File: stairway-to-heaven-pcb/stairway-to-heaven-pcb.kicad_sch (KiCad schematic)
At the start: 1 part, among them U1 MEGA_PRO_EMBED_CH340G_{slash}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

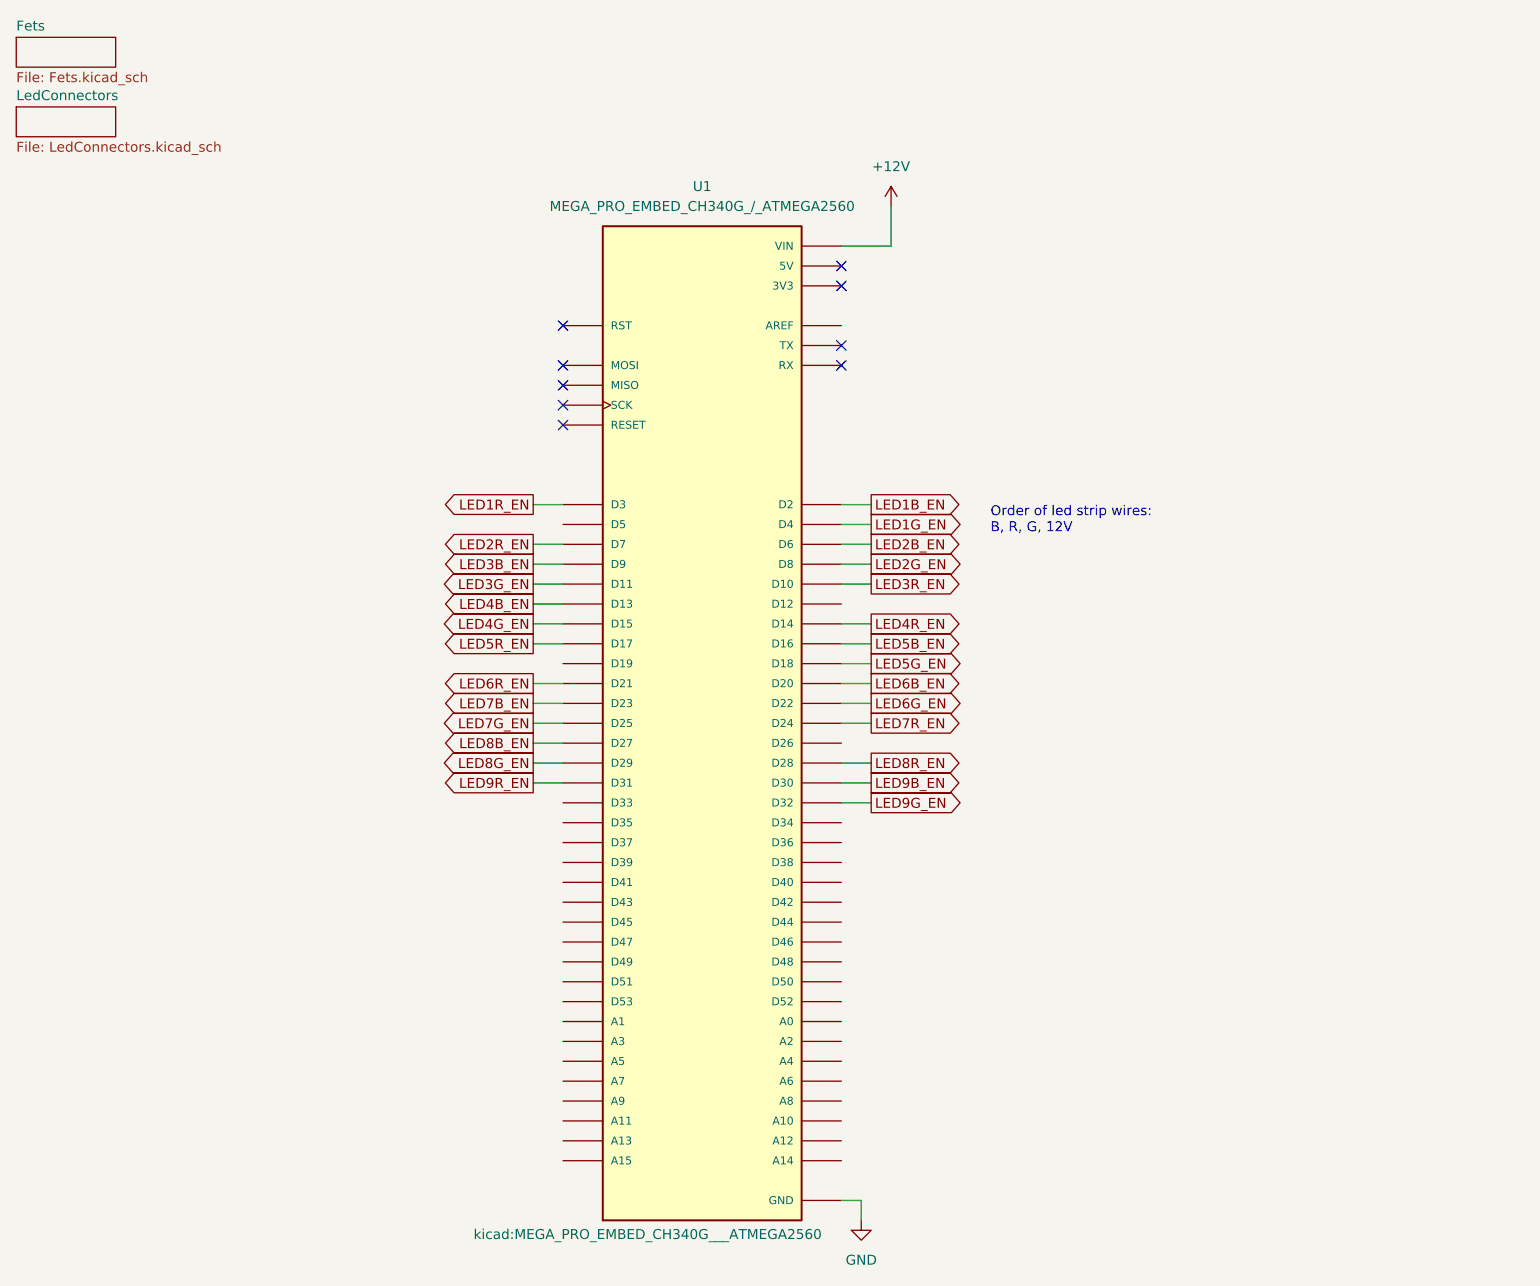
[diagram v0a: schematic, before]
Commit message: Psu, hierachical pages for fet driver
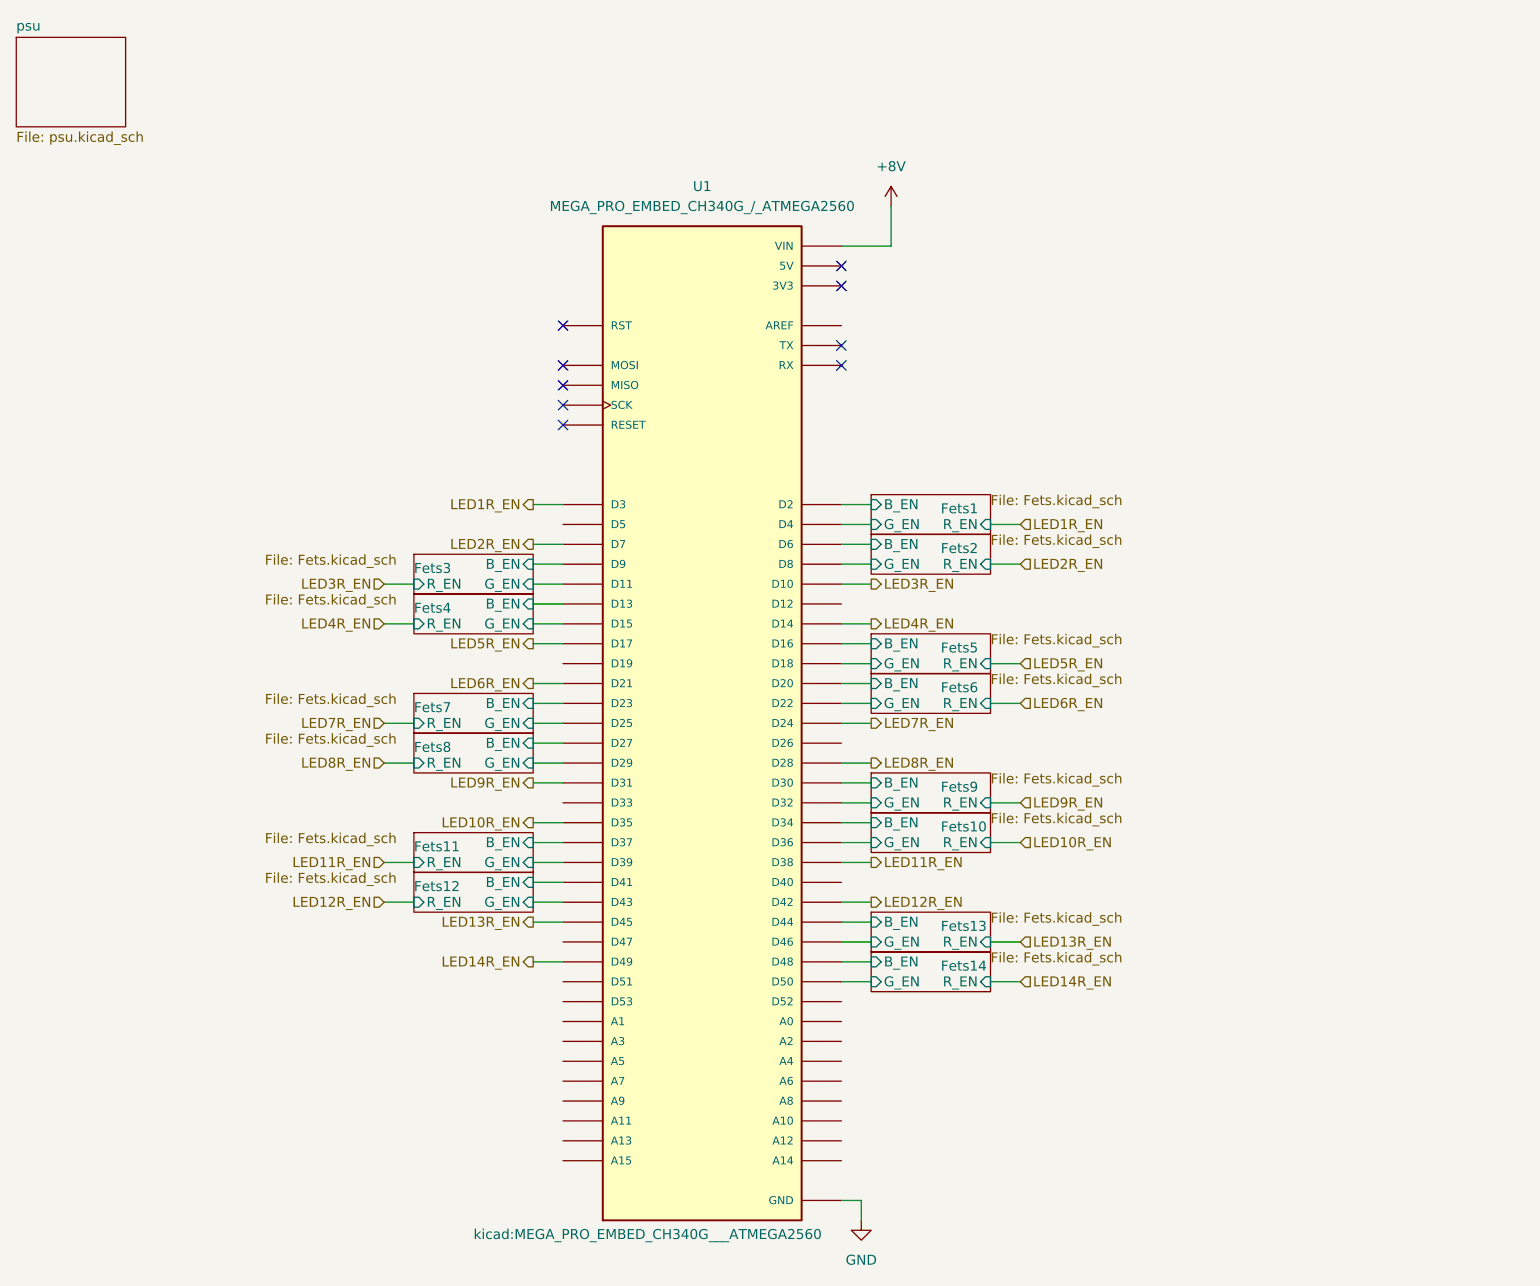
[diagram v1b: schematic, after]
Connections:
- net Fets10/B_EN: now reaches U1.D34
- net LED10R_EN: now reaches U1.D35
- net Fets10/G_EN: now reaches U1.D36
- net Fets11/B_EN: now reaches U1.D37
- net LED11R_EN: now reaches U1.D38
- net Fets11/G_EN: now reaches U1.D39
- net Fets12/B_EN: now reaches U1.D41
- net LED12R_EN: now reaches U1.D42
- net Fets12/G_EN: now reaches U1.D43
- net Fets13/B_EN: now reaches U1.D44
- net LED13R_EN: now reaches U1.D45
- net Fets13/G_EN: now reaches U1.D46
- net Fets14/B_EN: now reaches U1.D48
- net LED14R_EN: now reaches U1.D49
- net Fets14/G_EN: now reaches U1.D50
- net +12V renamed +8V
- net LED1B_EN renamed Fets1/B_EN
- net LED1G_EN renamed Fets1/G_EN
- net LED2B_EN renamed Fets2/B_EN
- net LED2G_EN renamed Fets2/G_EN
- net LED3B_EN renamed Fets3/B_EN
- net LED3G_EN renamed Fets3/G_EN
- net LED4B_EN renamed Fets4/B_EN
- net LED4G_EN renamed Fets4/G_EN
- net LED5B_EN renamed Fets5/B_EN
- net LED5G_EN renamed Fets5/G_EN
- net LED6B_EN renamed Fets6/B_EN
- net LED6G_EN renamed Fets6/G_EN
- net LED7B_EN renamed Fets7/B_EN
- net LED7G_EN renamed Fets7/G_EN
- net LED8B_EN renamed Fets8/B_EN
- net LED8G_EN renamed Fets8/G_EN
- net LED9B_EN renamed Fets9/B_EN
- net LED9G_EN renamed Fets9/G_EN
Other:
- sheet Fets renamed Fets1
- removed sheet LedConnectors
- added sheet Fets10 (Fets.kicad_sch)
- added sheet Fets11 (Fets.kicad_sch)
- added sheet Fets12 (Fets.kicad_sch)
- added sheet Fets13 (Fets.kicad_sch)
- added sheet Fets14 (Fets.kicad_sch)
- added sheet Fets2 (Fets.kicad_sch)
- added sheet Fets3 (Fets.kicad_sch)
- added sheet Fets4 (Fets.kicad_sch)
- added sheet Fets5 (Fets.kicad_sch)
- added sheet Fets6 (Fets.kicad_sch)
- added sheet Fets7 (Fets.kicad_sch)
- added sheet Fets8 (Fets.kicad_sch)
- added sheet Fets9 (Fets.kicad_sch)
- added sheet psu (psu.kicad_sch)
- sheet Fets1 ports: added B_EN, G_EN, R_EN; removed none
- note removed: "Order of led strip wires: B, R, G, 12V"

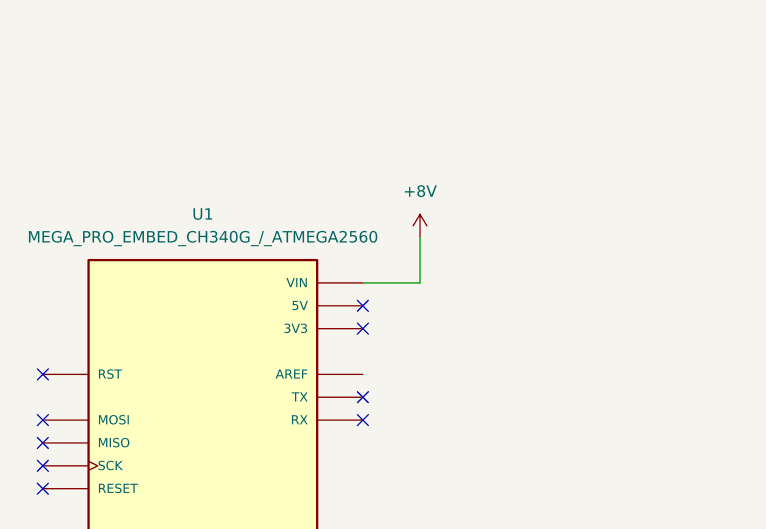
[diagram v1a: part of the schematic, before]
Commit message: DCDC from adj to 5V
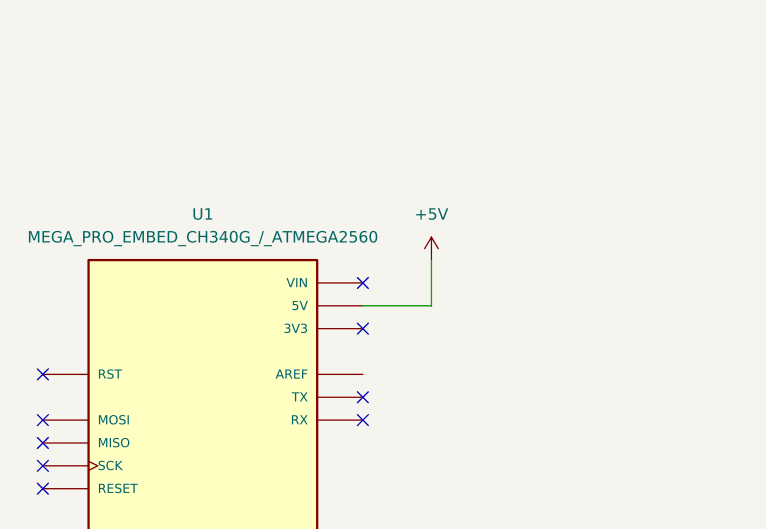
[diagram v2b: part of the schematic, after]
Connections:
- net +5V: now reaches U1.5V_1 (5V), U1.5V_2 (5V), U1.5V_3 (5V)
- net +8V: no longer names the net of U1.VIN_1 (VIN), U1.VIN_2 (VIN)
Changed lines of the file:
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@@
   (no_connect (at 85.09 53.34))
   (no_connect (at 120.65 48.26))
-  (no_connect (at 120.65 45.72))
   (no_connect (at 85.09 58.42))
   (no_connect (at 85.09 60.96))
+  (no_connect (at 120.65 43.18))
   (wire (pts (xy 139.7 78.74) (xy 143.51 78.74))
     (stroke (width 0) (type default) (color 0 0 0 0))
@@
     (stroke (width 0) (type default) (color 0 0 0 0))
   )
-  (wire (pts (xy 127 43.18) (xy 127 38.1))
-    (stroke (width 0) (type default) (color 0 0 0 0))
-  )
   (wire (pts (xy 139.7 101.6) (xy 143.51 101.6))
     (stroke (width 0) (type default) (color 0 0 0 0))
@@
     (stroke (width 0) (type default) (color 0 0 0 0))
   )
-  (wire (pts (xy 120.65 43.18) (xy 127 43.18))
-    (stroke (width 0) (type default) (color 0 0 0 0))
-  )
   (wire (pts (xy 81.28 91.44) (xy 85.09 91.44))
     (stroke (width 0) (type default) (color 0 0 0 0))
@@
     (stroke (width 0) (type default) (color 0 0 0 0))
   )
+  (wire (pts (xy 128.27 45.72) (xy 120.65 45.72))
+    (stroke (width 0) (type default) (color 0 0 0 0))
+  )
   (wire (pts (xy 62.23 86.36) (xy 66.04 86.36))
     (stroke (width 0) (type default) (color 0 0 0 0))
@@
   )
   (wire (pts (xy 81.28 86.36) (xy 85.09 86.36))
+    (stroke (width 0) (type default) (color 0 0 0 0))
+  )
+  (wire (pts (xy 128.27 40.64) (xy 128.27 45.72))
     (stroke (width 0) (type default) (color 0 0 0 0))
   )
@@
     (pin "VIN_2")
   )
-  (symbol (lib_id "power:+8V") (at 127 38.1 0) (unit 1)
+  (symbol (lib_id "power:+5V") (at 128.27 40.64 0) (unit 1)
     (in_bom yes) (on_board yes) (fields_autoplaced)
-    (property "Reference" "#PWR?" (id 0) (at 127 41.91 0)
+    (property "Reference" "#PWR?" (id 0) (at 128.27 44.45 0)
       (effects (font (size 1.27 1.27)) hide)
     )
-    (property "Value" "+8V" (id 1) (at 127 33.02 0))
-    (property "Footprint" "" (id 2) (at 127 38.1 0)
+    (property "Value" "+5V" (id 1) (at 128.27 35.56 0))
+    (property "Footprint" "" (id 2) (at 128.27 40.64 0)
       (effects (font (size 1.27 1.27)) hide)
     )
-    (property "Datasheet" "" (id 3) (at 127 38.1 0)
+    (property "Datasheet" "" (id 3) (at 128.27 40.64 0)
       (effects (font (size 1.27 1.27)) hide)
     )
@@
       (reference "#PWR0158") (unit 1) (value "+12V") (footprint "")
     )
+    (path "/c11913c3-97db-4bc4-9b11-925f21417dd2/2a4e254b-7c0c-4673-a8aa-40c6e531188f"
+      (reference "#PWR?") (unit 1) (value "+5V") (footprint "")
+    )
     (path "/c11913c3-97db-4bc4-9b11-925f21417dd2/2dbbf750-c1db-47bf-9f50-fe0096e42311"
       (reference "#PWR?") (unit 1) (value "GND") (footprint "")
     )
-    (path "/46daeb1d-2b42-43af-8d9c-b8a1e124ec13"
-      (reference "#PWR?") (unit 1) (value "+8V") (footprint "")
+    (path "/6eec8315-d166-4bd1-b370-f69e113e2d61"
+      (reference "#PWR?") (unit 1) (value "+5V") (footprint "")
     )
     (path "/c11913c3-97db-4bc4-9b11-925f21417dd2/c0053588-042a-47dc-a931-96eae35313ea"
@@
       (reference "#PWR?") (unit 1) (value "+12V") (footprint "")
     )
-    (path "/c11913c3-97db-4bc4-9b11-925f21417dd2/e1e8ab93-53e2-49b4-80f5-4568cb3bae24"
-      (reference "#PWR?") (unit 1) (value "+8V") (footprint "")
-    )
     (path "/c11913c3-97db-4bc4-9b11-925f21417dd2/21e0713d-6e7c-4f1e-bdd7-ce1b31e2fa5a"
       (reference "C?") (unit 1) (value "100uF") (footprint "")
     )
     (path "/c11913c3-97db-4bc4-9b11-925f21417dd2/d3ee5e22-3226-4c44-8f80-fd50ea4805fb"
-      (reference "C?") (unit 1) (value "1000uF") (footprint "")
-    )
-    (path "/c11913c3-97db-4bc4-9b11-925f21417dd2/11dc93c9-bf89-40e4-8c56-fa5713df8ffa"
-      (reference "D?") (unit 1) (value "D_Schottky") (footprint "")
+      (reference "C?") (unit 1) (value "330uF") (footprint "")
+    )
+    (path "/c11913c3-97db-4bc4-9b11-925f21417dd2/a5bc8825-a19e-48e0-b5c8-d712b25abbd3"
+      (reference "D?") (unit 1) (value "1N5819") (footprint "Diode_THT:D_DO-41_SOD81_P10.16mm_Horizontal")
     )
     (path "/c7e53204-9134-4b28-b397-09a3f9880698/c1eefc4b-76f4-40c3-b933-ab586706af53"
@@
       (reference "Q42") (unit 1) (value "FDN337N") (footprint "FDN337N:ON_Semi-527AG-01-12_2008-O-IPC_B")
     )
-    (path "/c11913c3-97db-4bc4-9b11-925f21417dd2/3510120f-b9d4-4bef-8743-b3c495a69b5b"
-      (reference "R?") (unit 1) (value "R") (footprint "Resistor_SMD:R_0805_2012Metric")
-    )
-    (path "/c11913c3-97db-4bc4-9b11-925f21417dd2/a88e6fef-131b-44ae-90d1-20b3e463b092"
-      (reference "R?") (unit 1) (value "R") (footprint "Resistor_SMD:R_0805_2012Metric")
-    )
     (path "/25cf98c8-de8d-4b21-86b9-2563caa0bbdb"
       (reference "U1") (unit 1) (value "MEGA_PRO_EMBED_CH340G_{slash}_ATMEGA2560") (footprint "kicad:MEGA_PRO_EMBED_CH340G___ATMEGA2560")
     )
-    (path "/c11913c3-97db-4bc4-9b11-925f21417dd2/97954bdd-6f0e-481b-b33b-a2801266daa9"
-      (reference "U?") (unit 1) (value "LM2576T-ADJG") (footprint "LM2576T-ADJG:LM2576T-ADJG")
-    )
-  )
+    (path "/c11913c3-97db-4bc4-9b11-925f21417dd2/e1e48912-b703-4c2a-a362-9c02ff10e8a1"
+      (reference "U?") (unit 1) (value "LM2575T-5.0") (footprint "kicad-ss-libs:LM2576T-ADJG")
+    )
+  )

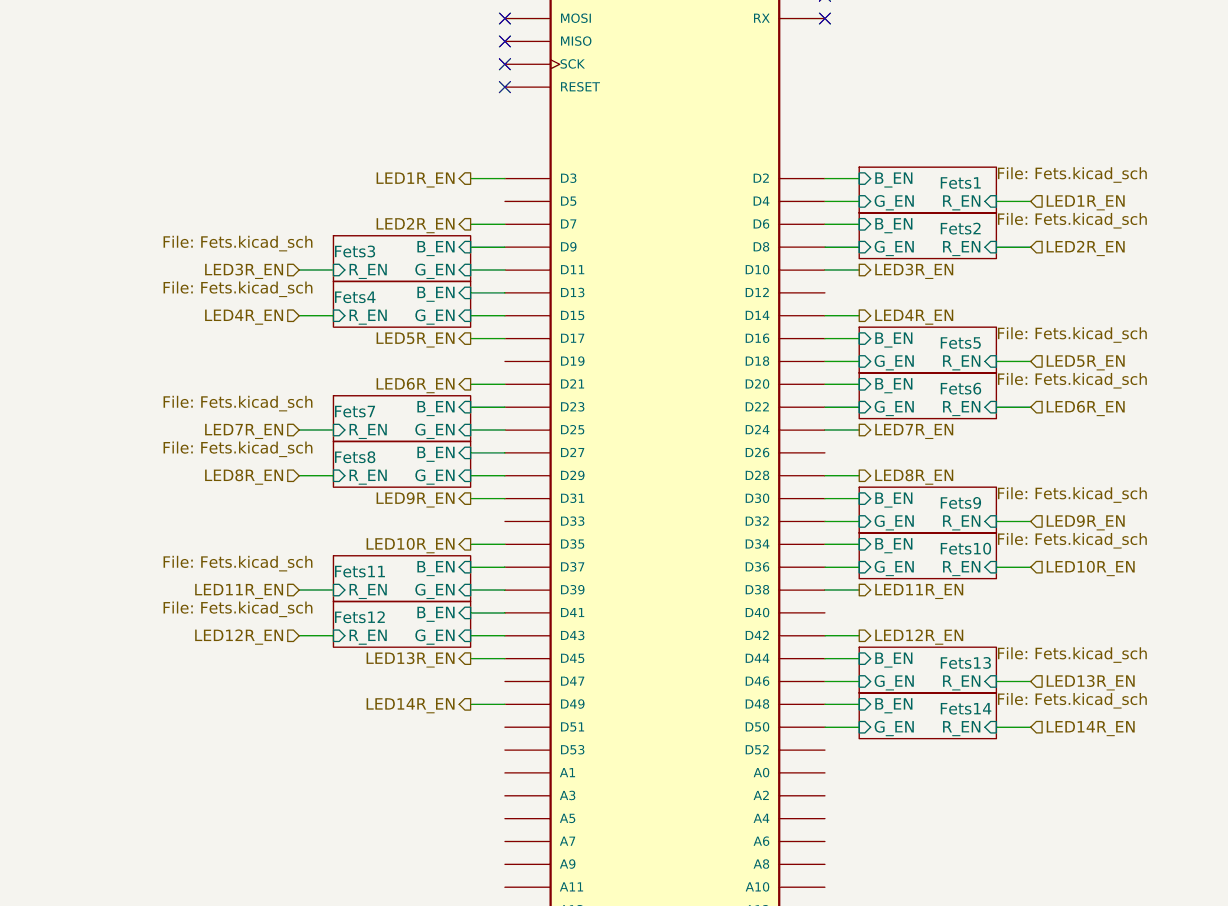
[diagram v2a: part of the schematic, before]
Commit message: initial pcb placement and routing tests
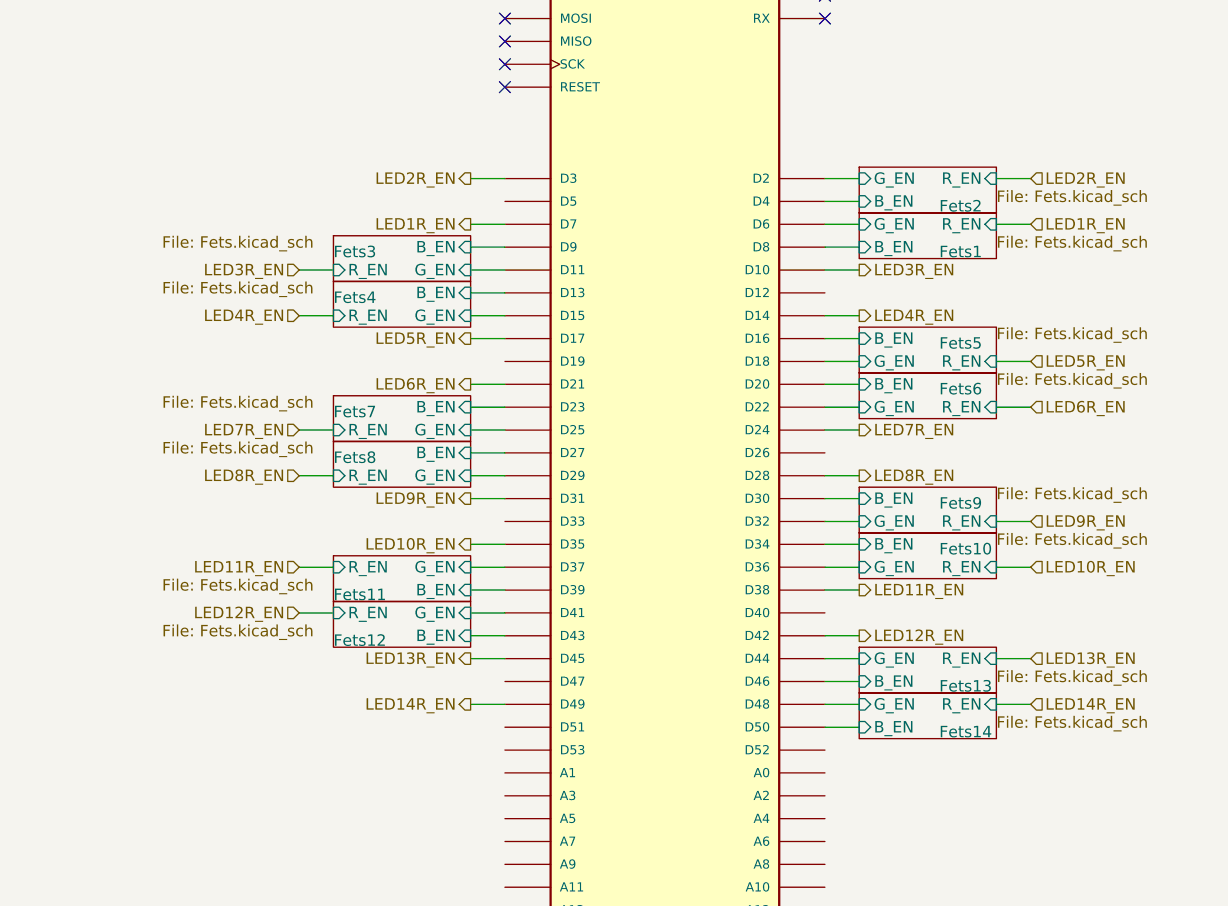
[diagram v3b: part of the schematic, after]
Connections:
- net Fets1/B_EN: now also U1.D8; no longer U1.D2
- net Fets1/G_EN: now also U1.D6; no longer U1.D4
- net Fets11/B_EN: now also U1.D39; no longer U1.D37
- net Fets11/G_EN: now also U1.D37; no longer U1.D39
- net Fets12/B_EN: now also U1.D43; no longer U1.D41
- net Fets12/G_EN: now also U1.D41; no longer U1.D43
- net Fets13/B_EN: now also U1.D46; no longer U1.D44
- net Fets13/G_EN: now also U1.D44; no longer U1.D46
- net Fets14/B_EN: now also U1.D50; no longer U1.D48
- net Fets14/G_EN: now also U1.D48; no longer U1.D50
- net Fets2/B_EN: now also U1.D4; no longer U1.D6
- net Fets2/G_EN: now also U1.D2; no longer U1.D8
- net LED1R_EN: now also U1.D7; no longer U1.D3
- net LED2R_EN: now also U1.D3; no longer U1.D7

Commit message: psu layout
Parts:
- added J15: PJ-063AH, kicad-ss-libs:CUI_PJ-063AH, symbol SS_connectors:PJ-063AH
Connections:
- net GND: now also J15.2, J15.S1 (SHIELD), J15.S2 (SHIELD)
- new net +12V: J15.1
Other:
- moved on the sheet: U1
